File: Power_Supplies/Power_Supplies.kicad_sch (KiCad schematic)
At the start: 0 parts

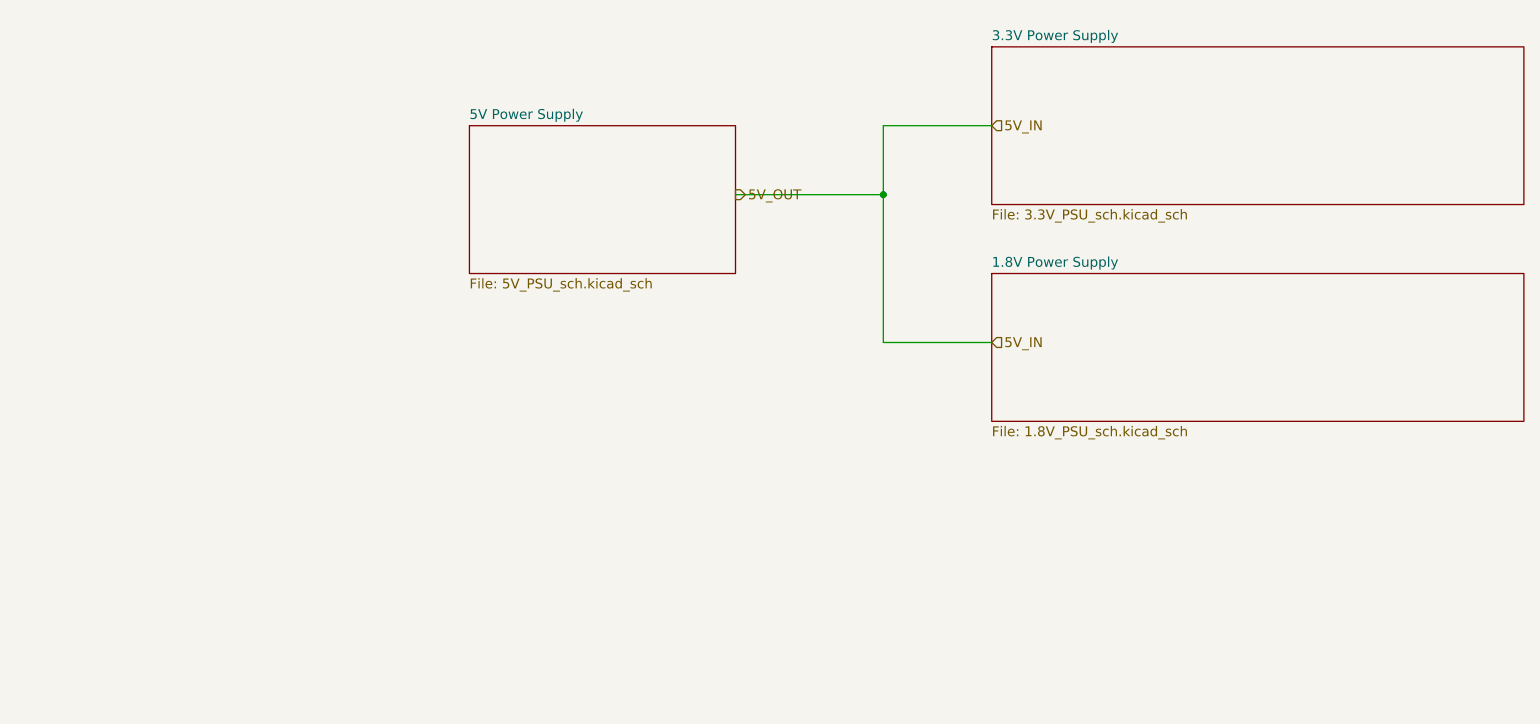
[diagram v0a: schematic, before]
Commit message: Updated power supplies and added DAC circuitry
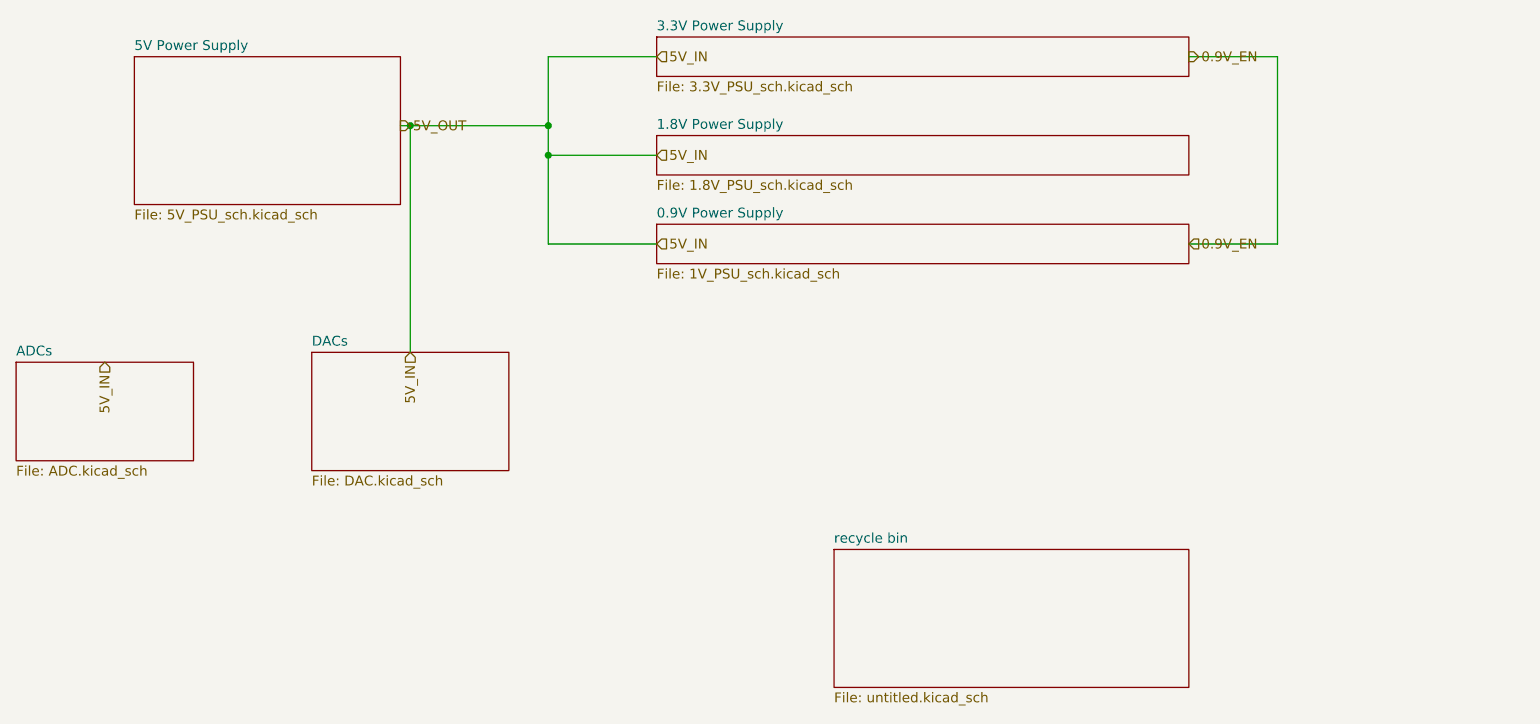
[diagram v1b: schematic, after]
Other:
- added sheet 0.9V Power Supply (1V_PSU_sch.kicad_sch)
- added sheet ADCs (ADC.kicad_sch)
- added sheet DACs (DAC.kicad_sch)
- added sheet recycle bin (untitled.kicad_sch)

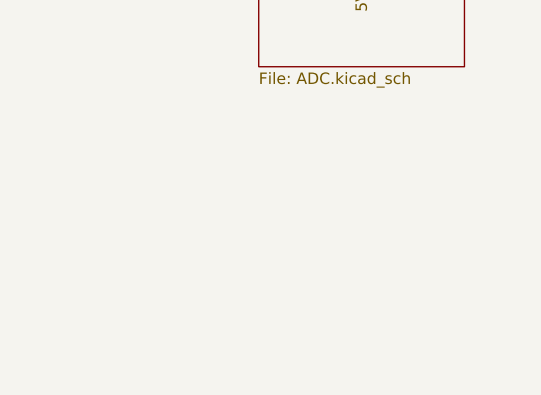
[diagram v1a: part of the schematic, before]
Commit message: Added xcore MCU, flash memory, main crystal clock
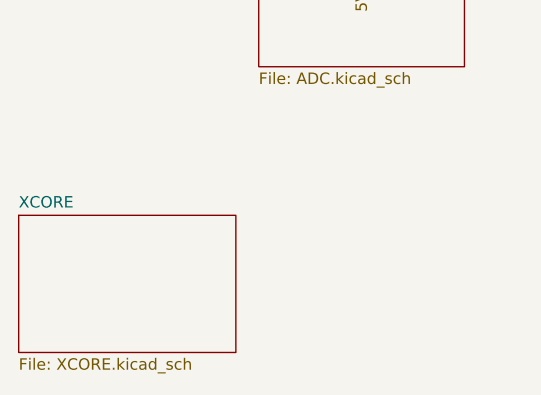
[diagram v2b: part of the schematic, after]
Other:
- added sheet XCORE (XCORE.kicad_sch)
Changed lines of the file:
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@@
+	)
+	(sheet
+		(at 39.37 90.17)
+		(size 24.13 15.24)
+		(fields_autoplaced yes)
+		(stroke
+			(width 0.1524)
+			(type solid)
+		)
+		(fill
+			(color 0 0 0 0.0000)
+		)
+		(property "Sheetname" "XCORE"
+			(at 39.37 89.4584 0)
+			(effects
+				(font
+					(size 1.27 1.27)
+				)
+				(justify left bottom)
+			)
+		)
+		(property "Sheetfile" "XCORE.kicad_sch"
+			(at 39.37 105.9946 0)
+			(effects
+				(font
+					(size 1.27 1.27)
+				)
+				(justify left top)
+			)
+		)
+		(instances
+			(project "Power_Supplies"
+				(path "/5266cf9e-da90-4c53-80fd-cf3dbed42632"
+					(page "9")
+				)
+			)
+		)
 	)
 	(sheet

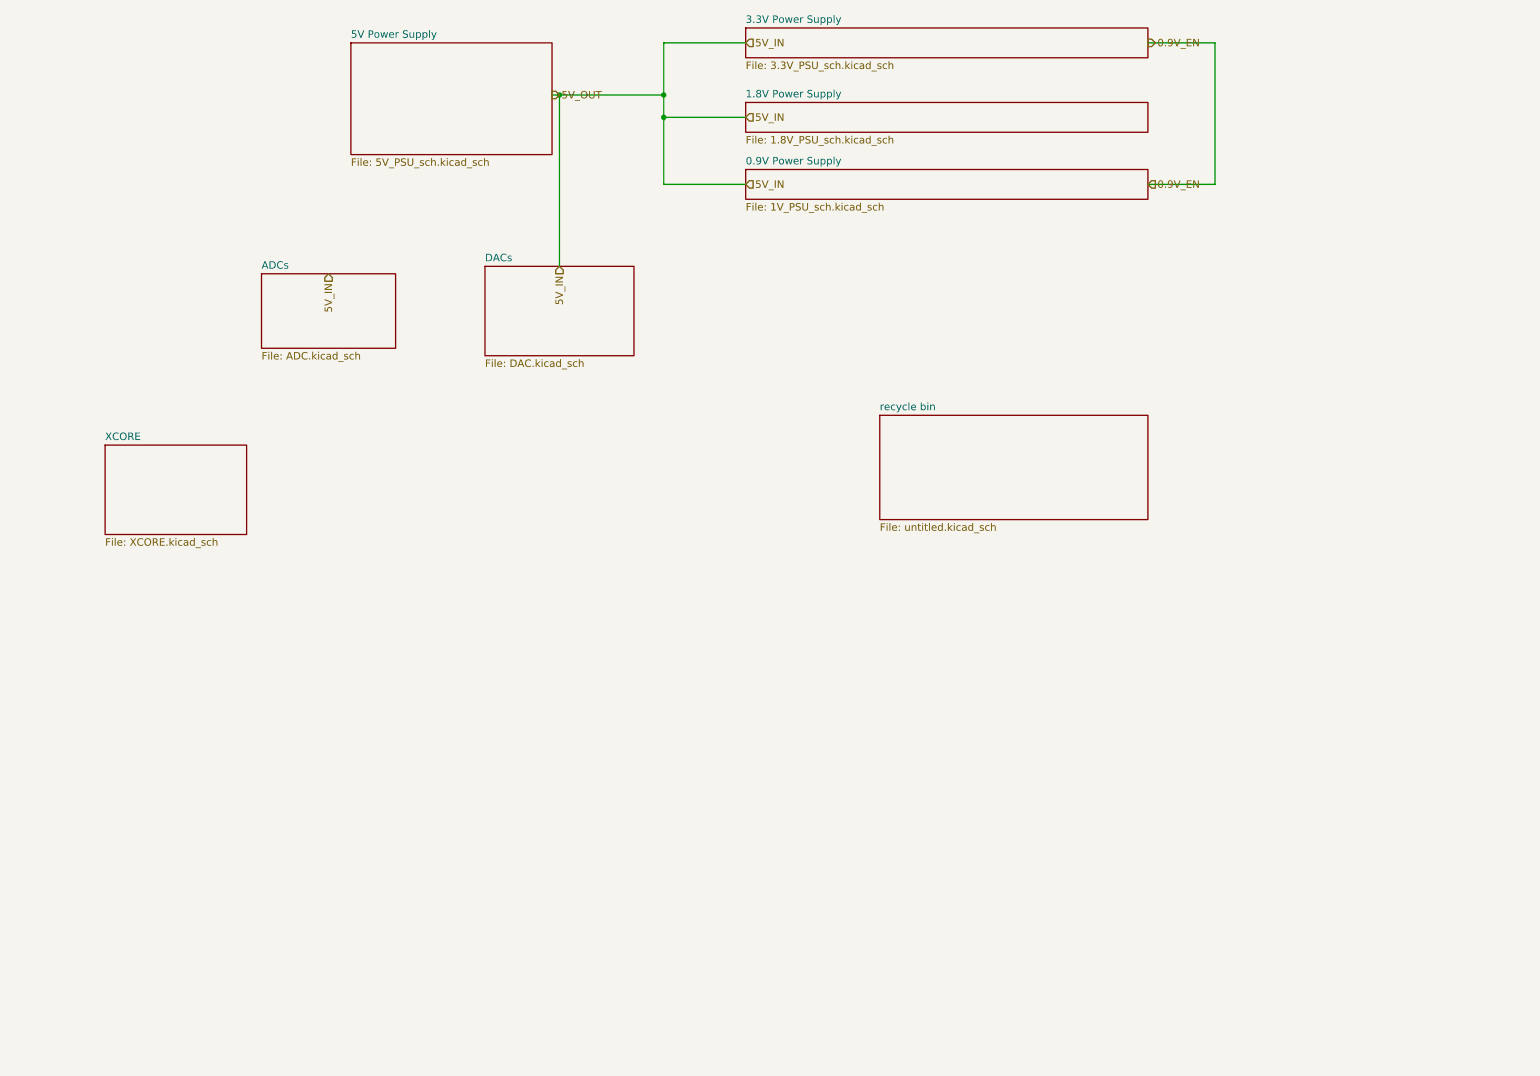
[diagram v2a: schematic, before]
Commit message: Added Phantom Power, updated Xcore library things
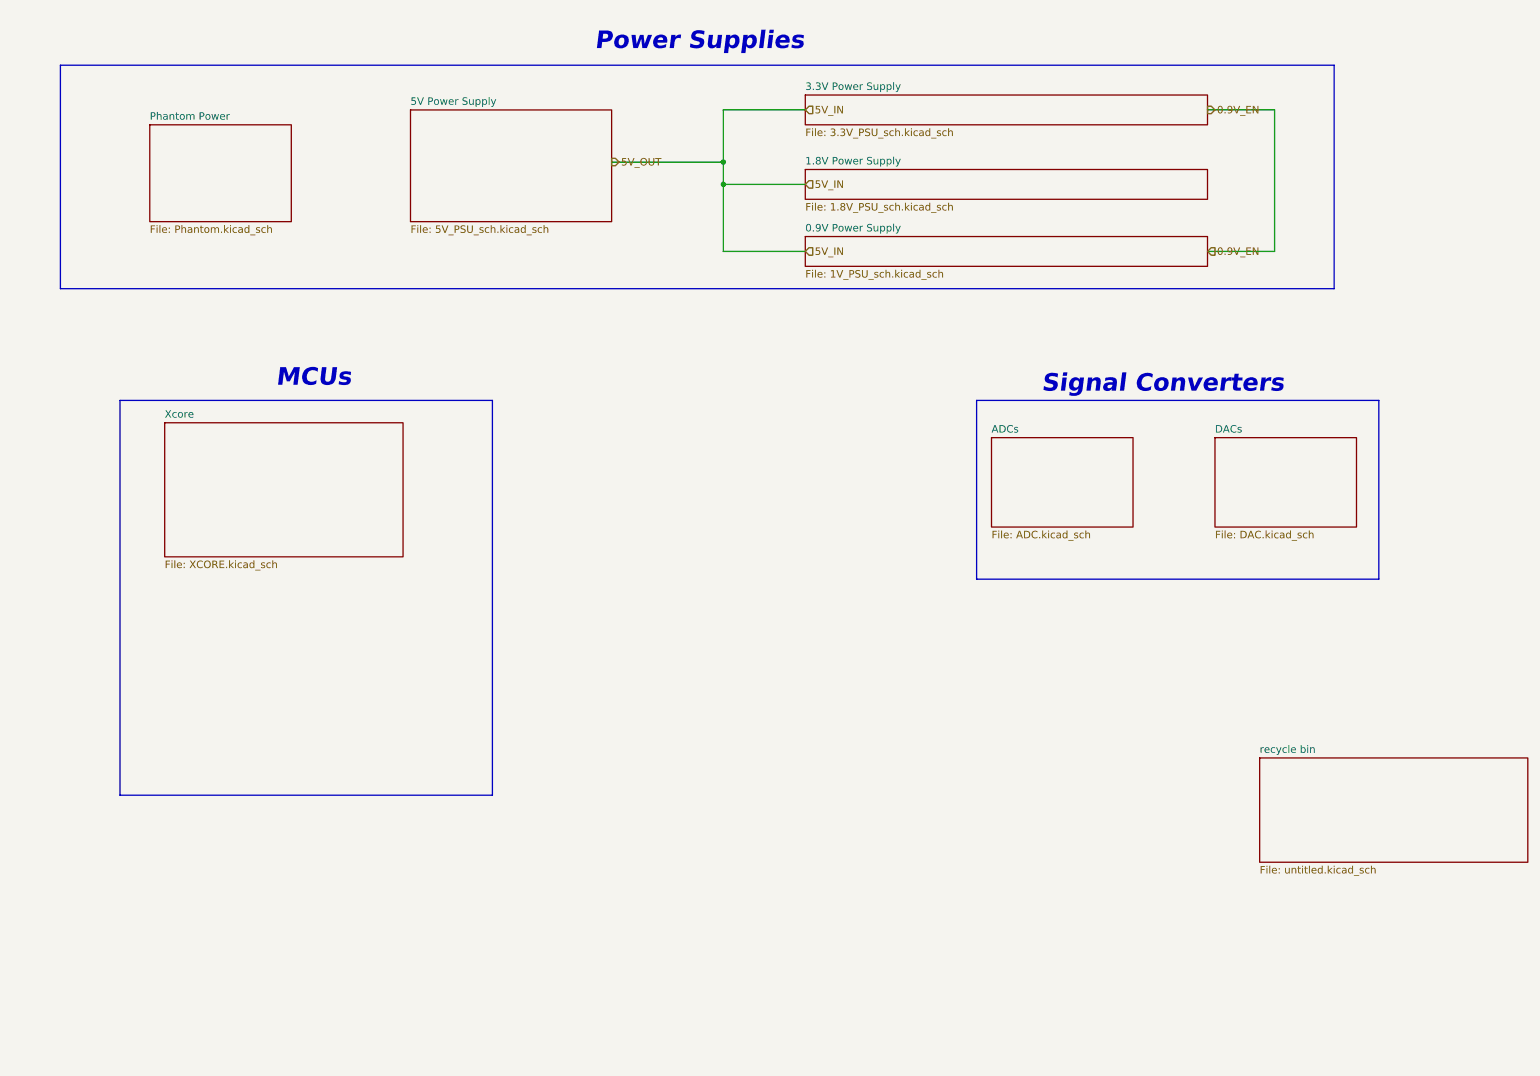
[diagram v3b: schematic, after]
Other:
- removed sheet XCORE
- added sheet Phantom Power (Phantom.kicad_sch)
- added sheet Xcore (XCORE.kicad_sch)
- note added: "MCUs"
- note added: "Power Supplies"
- note added: "Signal Converters"

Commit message: Started preamp design (finished stage 1)
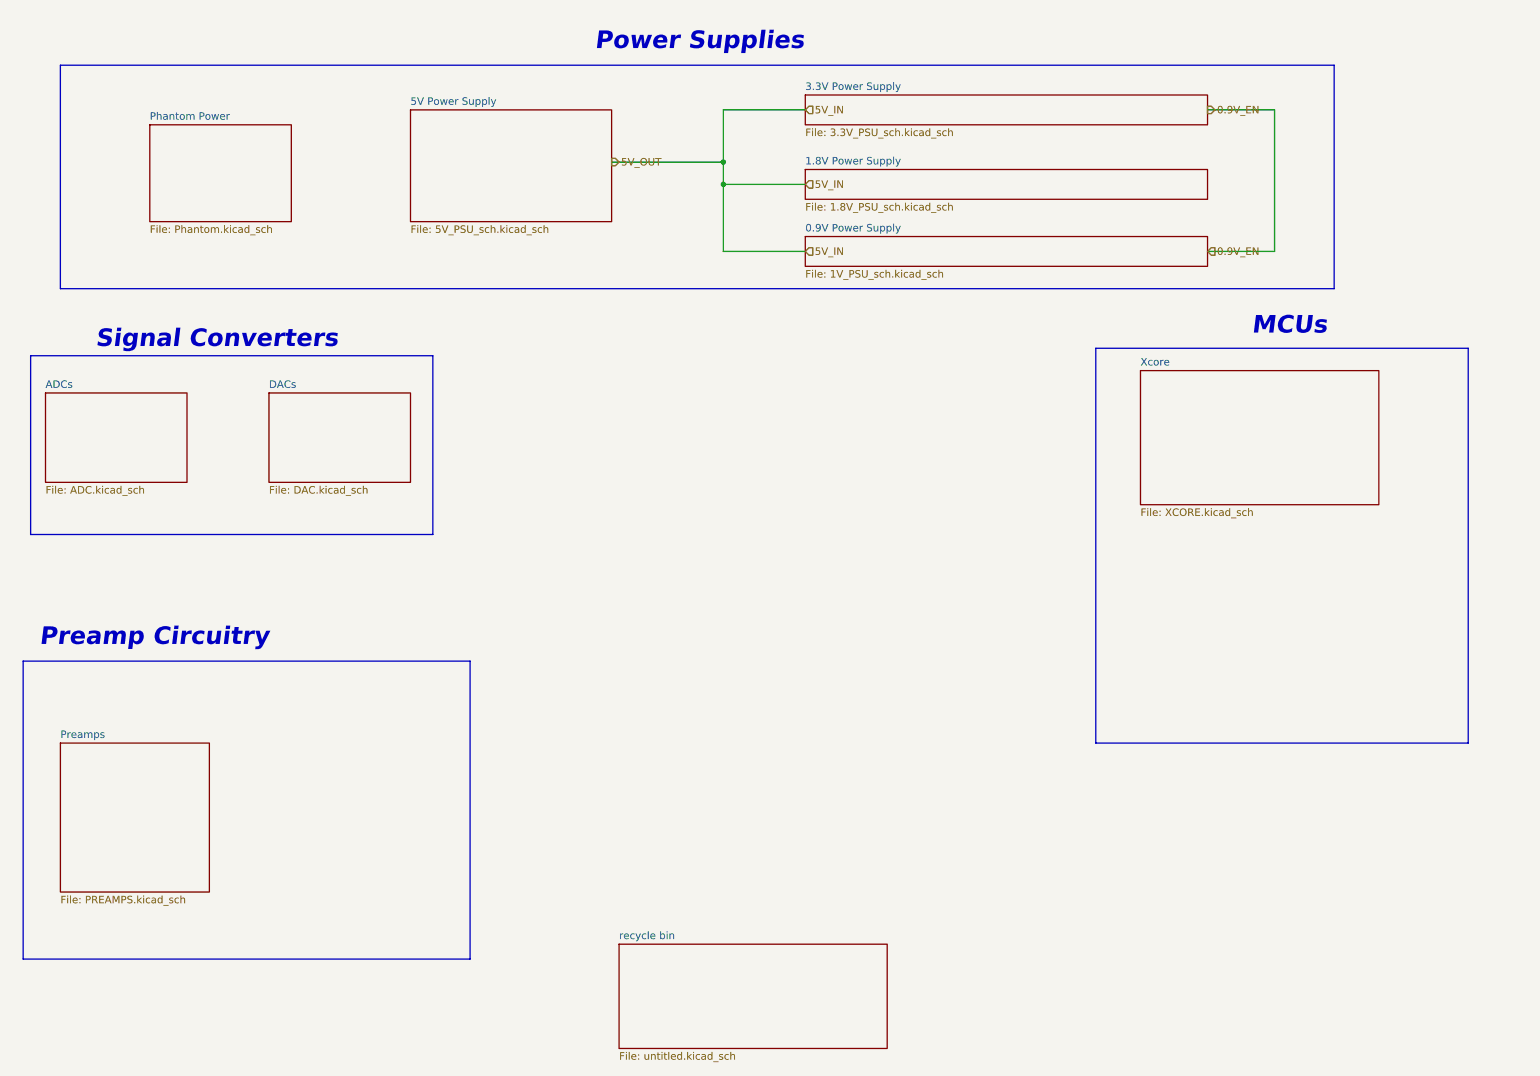
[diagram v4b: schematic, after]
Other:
- added sheet Preamps (PREAMPS.kicad_sch)
- note added: "Preamp Circuitry"
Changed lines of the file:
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@@
 	)
 	(rectangle
-		(start 187.96 82.55)
-		(end 256.54 113.03)
+		(start 26.67 74.93)
+		(end 95.25 105.41)
 		(stroke
 			(width 0)
@@
 	)
 	(rectangle
-		(start 41.91 82.55)
-		(end 105.41 149.86)
+		(start 208.28 73.66)
+		(end 271.78 140.97)
 		(stroke
 			(width 0)
@@
 		)
 	)
+	(rectangle
+		(start 25.4 127)
+		(end 101.6 177.8)
+		(stroke
+			(width 0)
+			(type default)
+		)
+		(fill
+			(type none)
+		)
+	)
 	(text "MCUs"
 		(exclude_from_sim no)
-		(at 74.93 78.74 0)
+		(at 241.3 69.85 0)
 		(effects
 			(font
@@
 	(text "Signal Converters"
 		(exclude_from_sim no)
-		(at 219.71 79.756 0)
+		(at 58.42 72.136 0)
 		(effects
 			(font
@@
 		)
 	)
+	(text "Preamp Circuitry\n"
+		(exclude_from_sim no)
+		(at 47.752 122.936 0)
+		(effects
+			(font
+				(size 3 3)
+				(thickness 0.6)
+				(bold yes)
+				(italic yes)
+			)
+		)
+	)
 	(hierarchical_label "5V_IN"
 		(shape input)
@@
 	)
 	(sheet
-		(at 228.6 88.9)
+		(at 67.31 81.28)
 		(size 24.13 15.24)
 		(fields_autoplaced yes)
@@
 		)
 		(property "Sheetname" "DACs"
-			(at 228.6 88.1884 0)
+			(at 67.31 80.5684 0)
 			(effects
 				(font
@@
 		)
 		(property "Sheetfile" "DAC.kicad_sch"
-			(at 228.6 104.7246 0)
+			(at 67.31 97.1046 0)
 			(effects
 				(font
@@
 	)
 	(sheet
-		(at 49.53 86.36)
+		(at 215.9 77.47)
 		(size 40.64 22.86)
 		(fields_autoplaced yes)
@@
 		)
 		(property "Sheetname" "Xcore"
-			(at 49.53 85.6484 0)
+			(at 215.9 76.7584 0)
 			(effects
 				(font
@@
 		)
 		(property "Sheetfile" "XCORE.kicad_sch"
-			(at 49.53 109.8046 0)
+			(at 215.9 100.9146 0)
 			(effects
 				(font
@@
 	)
 	(sheet
-		(at 190.5 88.9)
+		(at 29.21 81.28)
 		(size 24.13 15.24)
 		(fields_autoplaced yes)
@@
 		)
 		(property "Sheetname" "ADCs"
-			(at 190.5 88.1884 0)
+			(at 29.21 80.5684 0)
 			(effects
 				(font
@@
 		)
 		(property "Sheetfile" "ADC.kicad_sch"
-			(at 190.5 104.7246 0)
+			(at 29.21 97.1046 0)
 			(effects
 				(font
@@
 	)
 	(sheet
+		(at 31.75 140.97)
+		(size 25.4 25.4)
+		(fields_autoplaced yes)
+		(stroke
+			(width 0.1524)
+			(type solid)
+		)
+		(fill
+			(color 0 0 0 0.0000)
+		)
+		(property "Sheetname" "Preamps"
+			(at 31.75 140.2584 0)
+			(effects
+				(font
+					(size 1.27 1.27)
+				)
+				(justify left bottom)
+			)
+		)
+		(property "Sheetfile" "PREAMPS.kicad_sch"
+			(at 31.75 166.9546 0)
+			(effects
+				(font
+					(size 1.27 1.27)
+				)
+				(justify left top)
+			)
+		)
+		(instances
+			(project "Power_Supplies"
+				(path "/5266cf9e-da90-4c53-80fd-cf3dbed42632"
+					(page "11")
+				)
+			)
+		)
+	)
+	(sheet
 		(at 158.75 30.48)
 		(size 68.58 5.08)
@@
 	)
 	(sheet
-		(at 236.22 143.51)
+		(at 127 175.26)
 		(size 45.72 17.78)
 		(fields_autoplaced yes)
@@
 		)
 		(property "Sheetname" "recycle bin"
-			(at 236.22 142.7984 0)
+			(at 127 174.5484 0)
 			(effects
 				(font
@@
 		)
 		(property "Sheetfile" "untitled.kicad_sch"
-			(at 236.22 161.8746 0)
-			(effects
-				(font
+			(at 127 193.6246 0)
+			(effects
+				(font
